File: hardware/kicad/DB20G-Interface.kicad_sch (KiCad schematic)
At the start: 43 parts, among them J1 USB-C, J2 RADIO, J3 HANDSET, J4 DATA_PORT, K1 G5V-1-DC5, Q1 2N2222A, Q2 2N2222A, U1 FE1.1s, U2 CP2102N, U3 CM108AH, U4 AMS1117-3.3, Y1 12MHz

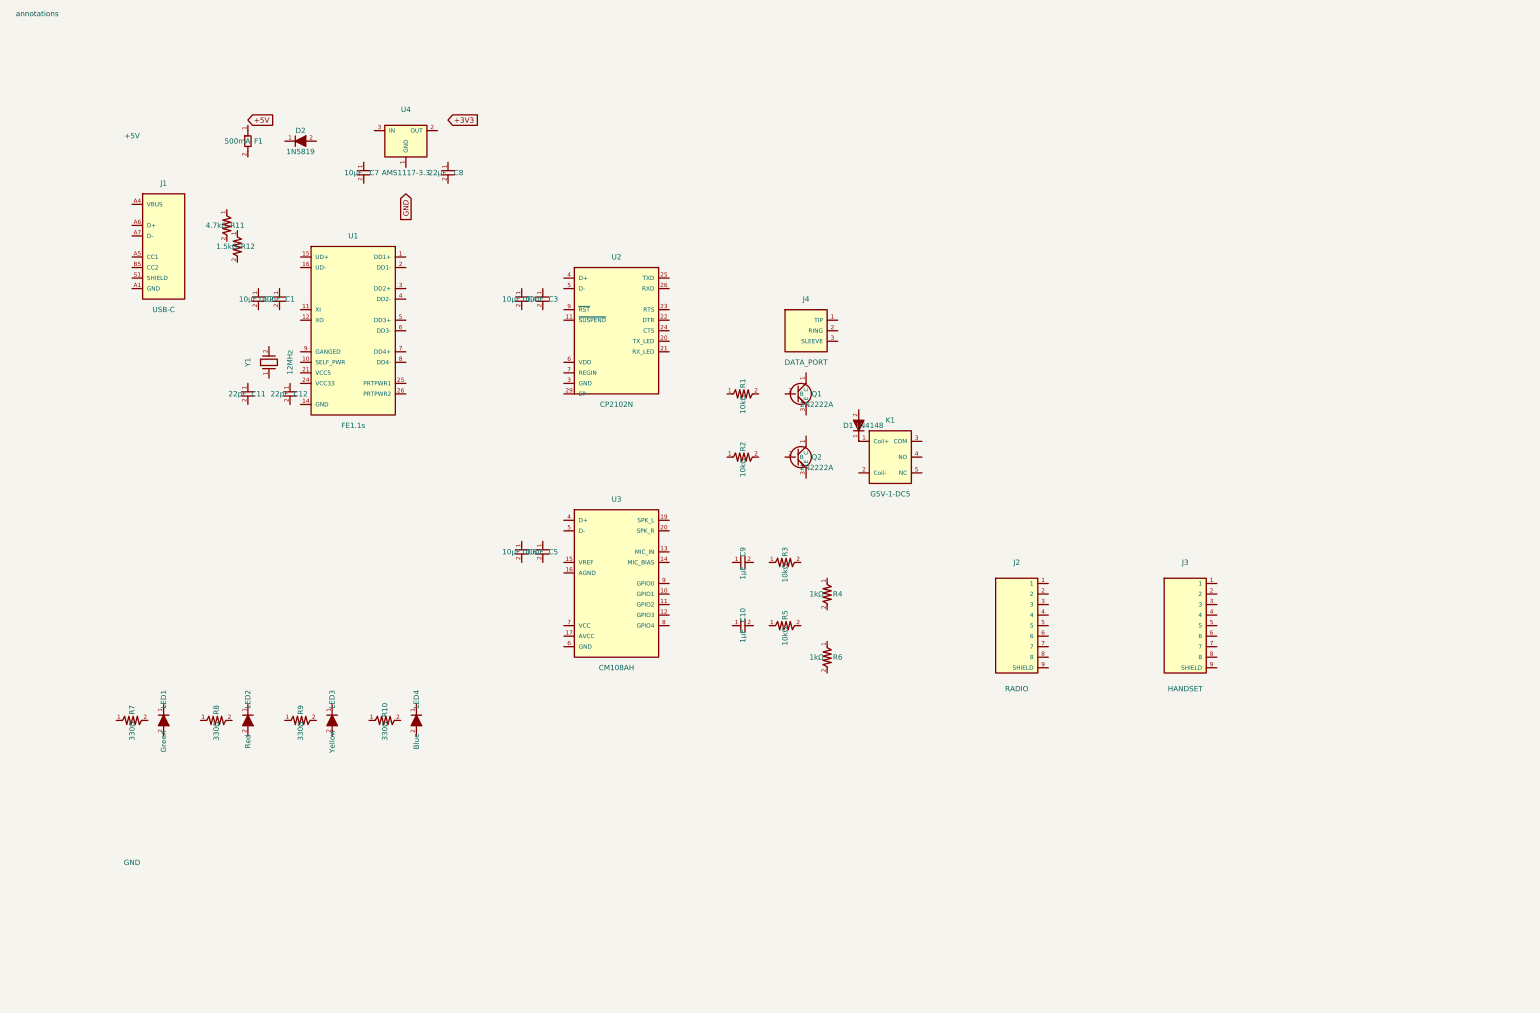
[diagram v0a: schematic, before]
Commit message: Revision to the Hardware interface
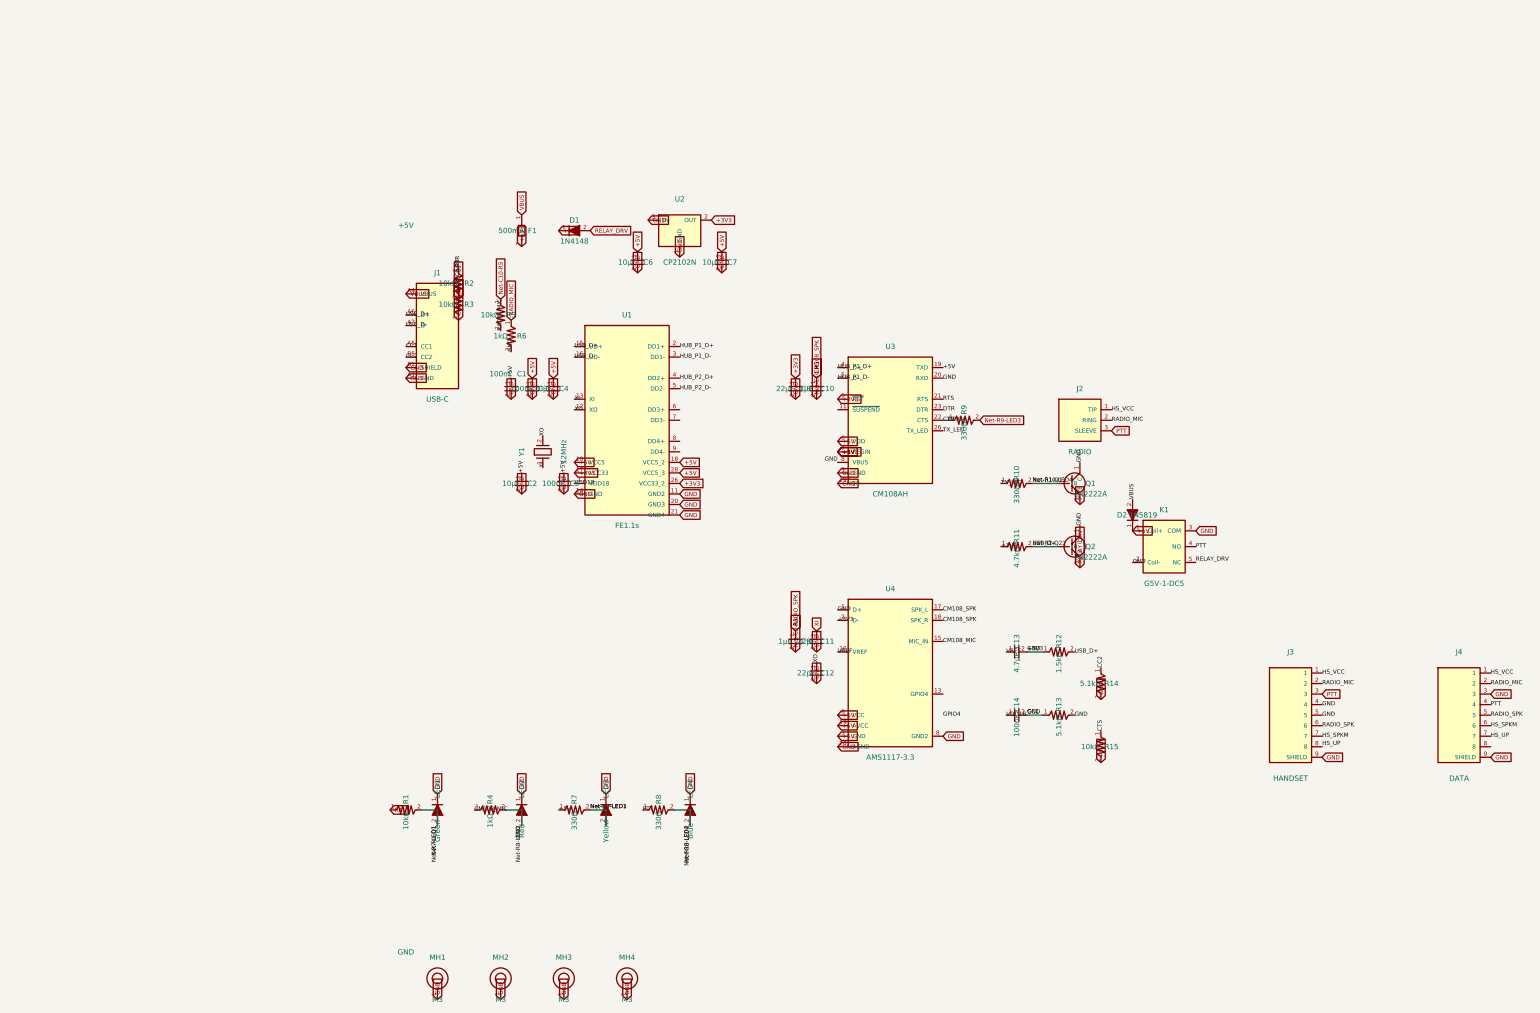
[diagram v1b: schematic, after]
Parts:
- removed J2: RADIO, symbol DB20G:RJ45
- removed J4: DATA_PORT, symbol DB20G:AudioJack3
- removed U2: CP2102N, symbol DB20G:CP2102N
- removed U3: CM108AH, symbol DB20G:CM108AH
- removed U4: AMS1117-3.3, symbol DB20G:AMS1117-3.3
- added C13: 4.7µF, Capacitor_SMD:C_0805_2012Metric, symbol DB20G:C
- added C14: 100nF, Capacitor_SMD:C_0805_2012Metric, symbol DB20G:C
- added J2: RADIO, Connector_RJ:RJ45_Amphenol_RJHSE5380, symbol DB20G:AudioJack3
- added J4: DATA, Connector_Audio:Jack_3.5mm_CUI_SJ1-3533NG_Horizontal, symbol DB20G:RJ45
- added MH1, MH2, MH3, MH4: M3, MountingHole:MountingHole_3.2mm_M3_Pad_Via, symbol DB20G:MountingHole_Pad
- added R13, R14: 5.1kΩ, Resistor_SMD:R_0805_2012Metric, symbol DB20G:R
- added R15: 10kΩ, Resistor_SMD:R_0805_2012Metric, symbol DB20G:R
- added U2: CP2102N, Package_DFN_QFN:QFN-28-1EP_5x5mm_P0.5mm_EP3.35x3.35mm, symbol DB20G:AMS1117-3.3
- added U3: CM108AH, Package_SO:SSOP-28_5.3x10.2mm_P0.65mm, symbol DB20G:CP2102N
- added U4: AMS1117-3.3, Package_TO_SOT_SMD:SOT-223-3_TabPin2, symbol DB20G:CM108AH
- C1, C10, C11, C12, C2, C3, C4, C5, C6, C7, C8, C9: footprint (none) -> Capacitor_SMD:C_0805_2012Metric
- D1, D2: footprint (none) -> Diode_SMD:D_SOD-123
- F1: footprint (none) -> Fuse:Fuse_1206_3216Metric
- J1: footprint (none) -> Connector_USB:USB_C_Receptacle_GCT_USB4105-xx-A_16P_TopMnt_Horizontal
- J3: footprint (none) -> Connector_RJ:RJ45_Amphenol_RJHSE5380
- K1: footprint (none) -> Relay_THT:Relay_SPDT_Omron_G5V-1
- LED1, LED2, LED3, LED4: footprint (none) -> LED_SMD:LED_0805_2012Metric
- Q1, Q2: footprint (none) -> Package_TO_SOT_THT:TO-92_Inline
- R1, R10, R11, R12, R2, R3, R4, R5, R6, R7, R8, R9: footprint (none) -> Resistor_SMD:R_0805_2012Metric
- U1: footprint (none) -> Package_SO:SSOP-28_5.3x10.2mm_P0.65mm
- Y1: footprint (none) -> Crystal:Crystal_HC49-U_Vertical
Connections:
- net +3V3: now also C1.1, C1.2, C11.2, C12.2, C2.1, C2.2, C3.1, C3.2, C4.1, C4.2, C5.1, C5.2, C6.1, C6.2, C7.1, C7.2, C8.1, C8.2, D1.1 (K), D2.1 (K), F1.2, J1.A1 (GND), J1.A5 (CC1), J1.S1 (SHIELD), J3.4, J3.5, J3.9 (SHIELD), K1.1 (Coil+), K1.2 (Coil-), K1.3 (COM), LED1.1 (K), LED1.2 (A), LED2.1 (K), LED2.2 (A), LED3.1 (K), LED3.2 (A), LED4.1 (K), LED4.2 (A), Q1.1 (C), Q1.2 (B), Q2.1 (C), R1.2, R10.2, R11.1, R12.1, R4.2, R6.2, R7.1, R7.2, R8.2, R9.2, U1.10 (VCC5), U1.11 (GND2), U1.14 (GND), U1.17 (VCC33), U1.18 (VCC5_2), U1.20 (GND3), U1.21 (GND4), U1.26 (VCC33_2), U1.28 (VCC5_3), C13.2, C14.2, J4.3, J4.9 (SHIELD), MH1.1, MH2.1, MH3.1, MH4.1, R13.1, R13.2, R14.2, R15.2, U2.1 (GND), U2.2 (OUT), U2.3 (IN), U3.19 (TXD), U3.20 (RXD), U3.29 (EP), U3.3 (GND), U3.6 (VDD), U3.7 (REGIN), U3.8 (VBUS), U3.9 (~{RST}), U4.1 (D+), U4.19 (AVCC), U4.2 (D-), U4.20 (AGND), U4.3 (GND), U4.6 (VCC), U4.8 (GND2)
- net CM108_SPK: now reaches C10.1
- net CM108_SPK: now also U4.17 (SPK_L), U4.18 (SPK_R)
- net Net-C10-R5: now reaches C10.2
- net Net-C10-R5: now also R5.1
- net XI: now reaches C11.1
- net XI: now also U1.13 (XI), Y1.1
- net XO: now reaches C12.1
- net XO: now also U1.12 (XO), Y1.2
- net RADIO_SPK: now reaches C9.1
- net RADIO_SPK: now also J3.6, J4.5
- net Net-C9-R3: now reaches C9.2
- net Net-C9-R3: now also R3.1
- net RELAY_DRV: now reaches D1.2 (A)
- net RELAY_DRV: now also K1.5 (NC), Q2.3 (E)
- net VBUS: now reaches D2.2 (A)
- net VBUS: now also F1.1, J1.A4 (VBUS)
- net Net-R2-Q2: now reaches J1.A6 (D+)
- net Net-R2-Q2: now also Q2.2 (B), R11.2, R12.2, R2.2, U1.15 (UD+)
- net USB_D-: now reaches J1.A7 (D-)
- net USB_D-: now also U1.16 (UD-)
- net CC2: now reaches J1.B5 (CC2)
- net CC2: now also R14.1
- net HS_VCC: now reaches J3.1
- net HS_VCC: now also J2.1 (TIP), J4.1
- net RADIO_MIC: now reaches J3.2
- net RADIO_MIC: now also R5.2, R6.1, J2.2 (RING), J4.2
- net PTT: now reaches J3.3
- net PTT: now also K1.4 (NO), Q1.3 (E), R8.1, J2.3 (SLEEVE), J4.4
- net HS_SPKM: now reaches J3.7
- net HS_SPKM: now also J4.6
- net HS_UP: now reaches J3.8
- net HS_UP: now also J4.7
- net RTS: now reaches R1.1
- net RTS: now also U3.21 (RTS)
- net TX_LED: now reaches R10.1
- net TX_LED: now also U3.26 (TX_LED)
- net DTR: now reaches R2.1
- net DTR: now also U3.23 (DTR)
- net CM108_MIC: now reaches R3.2
- net CM108_MIC: now also R4.1, U4.15 (MIC_IN)
- net CTS: now reaches R9.1
- net CTS: now also R15.1, U3.22 (CTS)
- net VDD18: now reaches U1.1 (VDD18)
- net VDD18: now also C14.1
- net HUB_P1_D+: now reaches U1.2 (DD1+)
- net HUB_P1_D+: now also U3.4 (D+)
- net HUB_P1_D-: now reaches U1.3 (DD1-)
- net HUB_P1_D-: now also U3.5 (D-)
- net HUB_P2_D+: now reaches U1.4 (DD2+)
- net HUB_P2_D-: now reaches U1.5 (DD2-)
- new net VREF: C13.1, U4.16 (VREF)
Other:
- note removed: "annotations"
